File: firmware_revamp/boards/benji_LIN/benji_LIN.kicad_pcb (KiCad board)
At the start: 2 copper layers, 42.9 x 81 mm, 39 parts, among them J1 CONN_02X03, J2 Conn_01x11, J3 Conn_01x11, J4 CONN_01X03, J5 CONN_01x02, J6 CONN_01X03, J7 CONN_01x02, U1 MCP2561-E_SN, U2 ATMEGA16M1, U3 TLIN1021DRQ1, Y1 Crystal_SMD

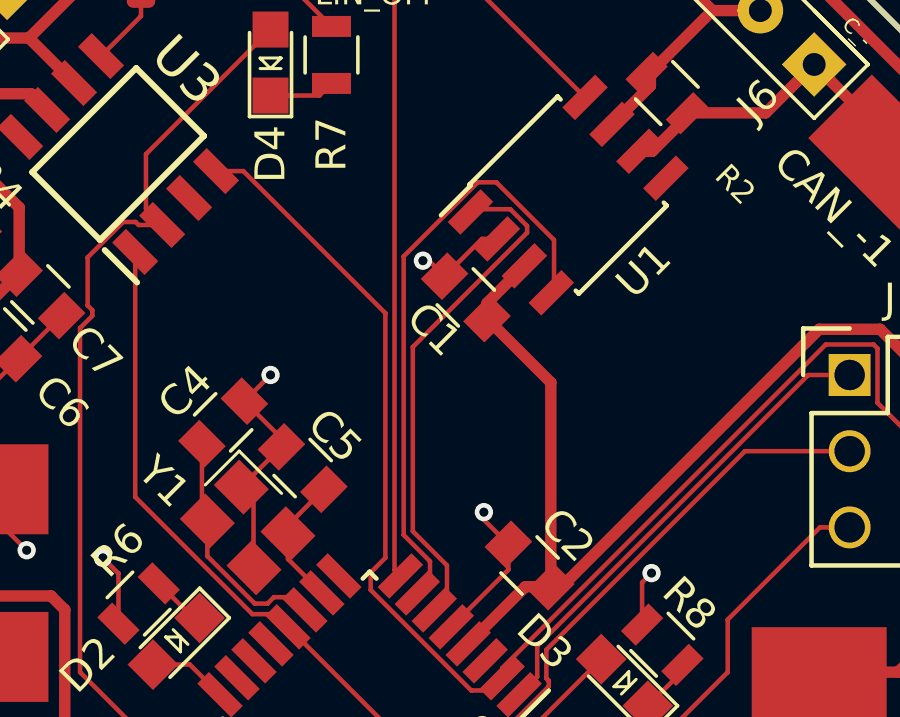
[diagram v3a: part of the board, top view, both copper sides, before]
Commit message: fixed GND via placement
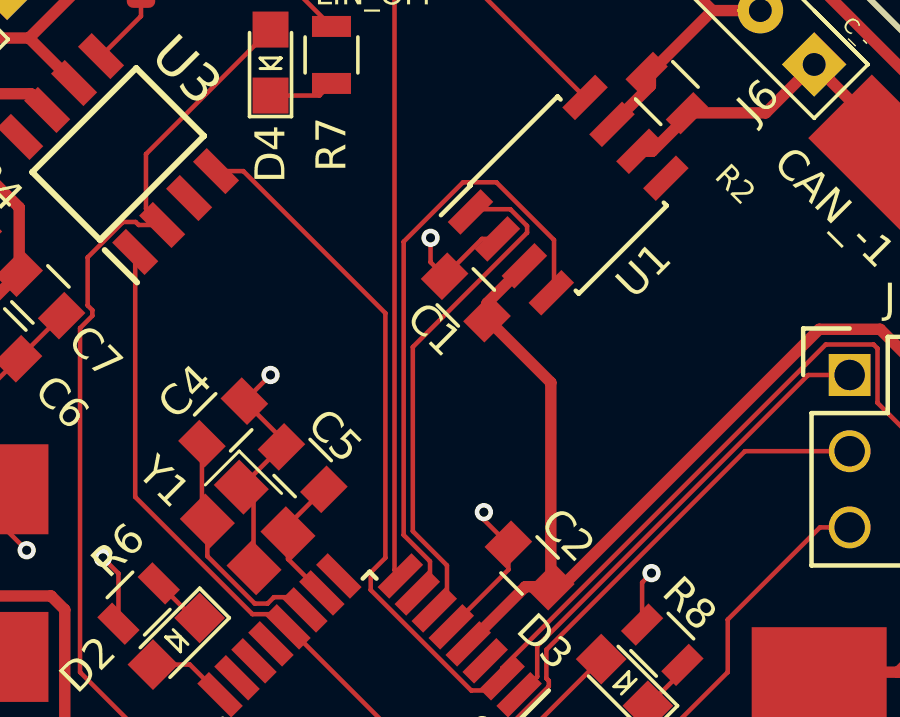
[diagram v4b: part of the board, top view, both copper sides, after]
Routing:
- net GND: track 61.7 -> 62.2 mm
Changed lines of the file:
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@@
   )
   (setup
-    (last_trace_width 0.381)
+    (last_trace_width 0.1524)
     (user_trace_width 0.254)
     (user_trace_width 0.381)
@@
   (via (at 97.028 81.28) (size 0.6096) (drill 0.3048) (layers F.Cu B.Cu) (net 1))
   (via (at 105.156 75.438) (size 0.6096) (drill 0.3048) (layers F.Cu B.Cu) (net 1))
-  (via (at 110.236 71.628) (size 0.6096) (drill 0.3048) (layers F.Cu B.Cu) (net 1))
+  (via (at 110.49 70.866) (size 0.6096) (drill 0.3048) (layers F.Cu B.Cu) (net 1))
   (segment (start 112.203218 70.901485) (end 112.719406 70.901485) (width 0.1524) (layer F.Cu) (net 1))
   (segment (start 110.958003 72.1467) (end 112.203218 70.901485) (width 0.1524) (layer F.Cu) (net 1))
@@
   (segment (start 104.589654 81.845025) (end 104.589654 79.582283) (width 0.1524) (layer F.Cu) (net 1))
   (segment (start 104.606132 81.861503) (end 104.589654 81.845025) (width 0.1524) (layer F.Cu) (net 1))
-  (segment (start 110.439303 71.628) (end 110.958003 72.1467) (width 0.1524) (layer F.Cu) (net 1))
-  (segment (start 110.236 71.628) (end 110.439303 71.628) (width 0.1524) (layer F.Cu) (net 1))
   (segment (start 104.284214 76.309786) (end 105.156 75.438) (width 0.1524) (layer F.Cu) (net 1))
   (segment (start 96.755151 74.896553) (end 98.191992 73.459712) (width 0.1524) (layer F.Cu) (net 1))
@@
   (segment (start 117.541921 82.356079) (end 117.856 82.042) (width 0.1524) (layer F.Cu) (net 1))
   (segment (start 117.541921 83.757746) (end 117.541921 82.356079) (width 0.1524) (layer F.Cu) (net 1))
+  (segment (start 110.49 71.678697) (end 110.958003 72.1467) (width 0.1524) (layer F.Cu) (net 1))
+  (segment (start 110.49 70.866) (end 110.49 71.678697) (width 0.1524) (layer F.Cu) (net 1))
   (segment (start 113.650579 82.495107) (end 111.746047 84.399639) (width 0.381) (layer F.Cu) (net 2))
   (segment (start 114.499107 82.495107) (end 113.650579 82.495107) (width 0.381) (layer F.Cu) (net 2))
@@
   (segment (start 125.73 67.539395) (end 125.73 68.072) (width 0.381) (layer F.Cu) (net 26))
   (segment (start 123.277812 65.087207) (end 125.73 67.539395) (width 0.381) (layer F.Cu) (net 26))
+  (segment (start 109.593661 80.772) (end 110.472055 81.650394) (width 0.1524) (layer F.Cu) (net 28))
+  (segment (start 111.573108 69.01471) (end 109.593661 70.994157) (width 0.1524) (layer F.Cu) (net 28))
+  (segment (start 112.683016 69.01471) (end 111.573108 69.01471) (width 0.1524) (layer F.Cu) (net 28))
   (segment (start 110.472055 81.650394) (end 110.472055 82.279518) (width 0.1524) (layer F.Cu) (net 28))
-  (segment (start 109.593661 80.772) (end 110.472055 81.650394) (width 0.1524) (layer F.Cu) (net 28))
-  (segment (start 112.06256 69.01471) (end 109.593661 71.483609) (width 0.1524) (layer F.Cu) (net 28))
-  (segment (start 112.683016 69.01471) (end 112.06256 69.01471) (width 0.1524) (layer F.Cu) (net 28))
   (segment (start 114.606181 70.937875) (end 112.683016 69.01471) (width 0.1524) (layer F.Cu) (net 28))
   (segment (start 110.472055 82.279518) (end 110.04899 82.702583) (width 0.1524) (layer F.Cu) (net 28))
-  (segment (start 109.593661 71.483609) (end 109.593661 80.772) (width 0.1524) (layer F.Cu) (net 28))
   (segment (start 114.606181 72.606813) (end 114.606181 70.937875) (width 0.1524) (layer F.Cu) (net 28))
+  (segment (start 109.593661 70.994157) (end 109.593661 80.772) (width 0.1524) (layer F.Cu) (net 28))
   (segment (start 114.515457 72.697537) (end 114.606181 72.606813) (width 0.1524) (layer F.Cu) (net 28))
   (segment (start 110.614676 83.187324) (end 110.614676 83.268268) (width 0.1524) (layer F.Cu) (net 29))

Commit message: Finished Ratsnest connections
semifinal version 1.1 commit
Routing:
- net GND: track 62.2 -> 72.8 mm
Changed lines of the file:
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@@
     (thickness 1.6)
     (drawings 22)
-    (tracks 305)
+    (tracks 308)
     (zones 0)
     (modules 39)
@@
   (segment (start 110.49 71.678697) (end 110.958003 72.1467) (width 0.1524) (layer F.Cu) (net 1))
   (segment (start 110.49 70.866) (end 110.49 71.678697) (width 0.1524) (layer F.Cu) (net 1))
+  (segment (start 114.554 102.87) (end 113.284 101.6) (width 0.1524) (layer F.Cu) (net 1))
+  (segment (start 113.284 97.536) (end 116.676249 94.143751) (width 0.1524) (layer F.Cu) (net 1))
+  (segment (start 113.284 101.6) (end 113.284 97.536) (width 0.1524) (layer F.Cu) (net 1))
   (segment (start 113.650579 82.495107) (end 111.746047 84.399639) (width 0.381) (layer F.Cu) (net 2))
   (segment (start 114.499107 82.495107) (end 113.650579 82.495107) (width 0.381) (layer F.Cu) (net 2))

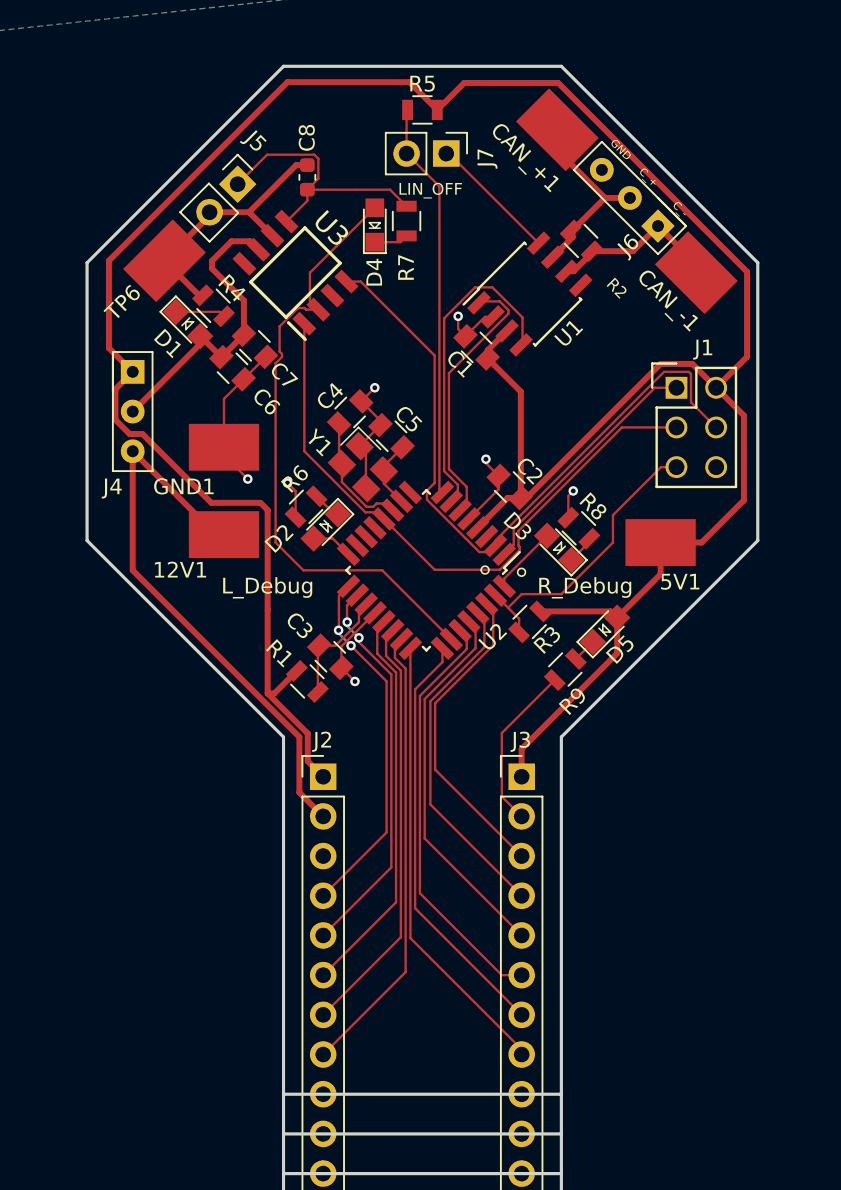
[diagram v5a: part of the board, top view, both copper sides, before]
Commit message: Rearranged mostly visual errors, removed diode
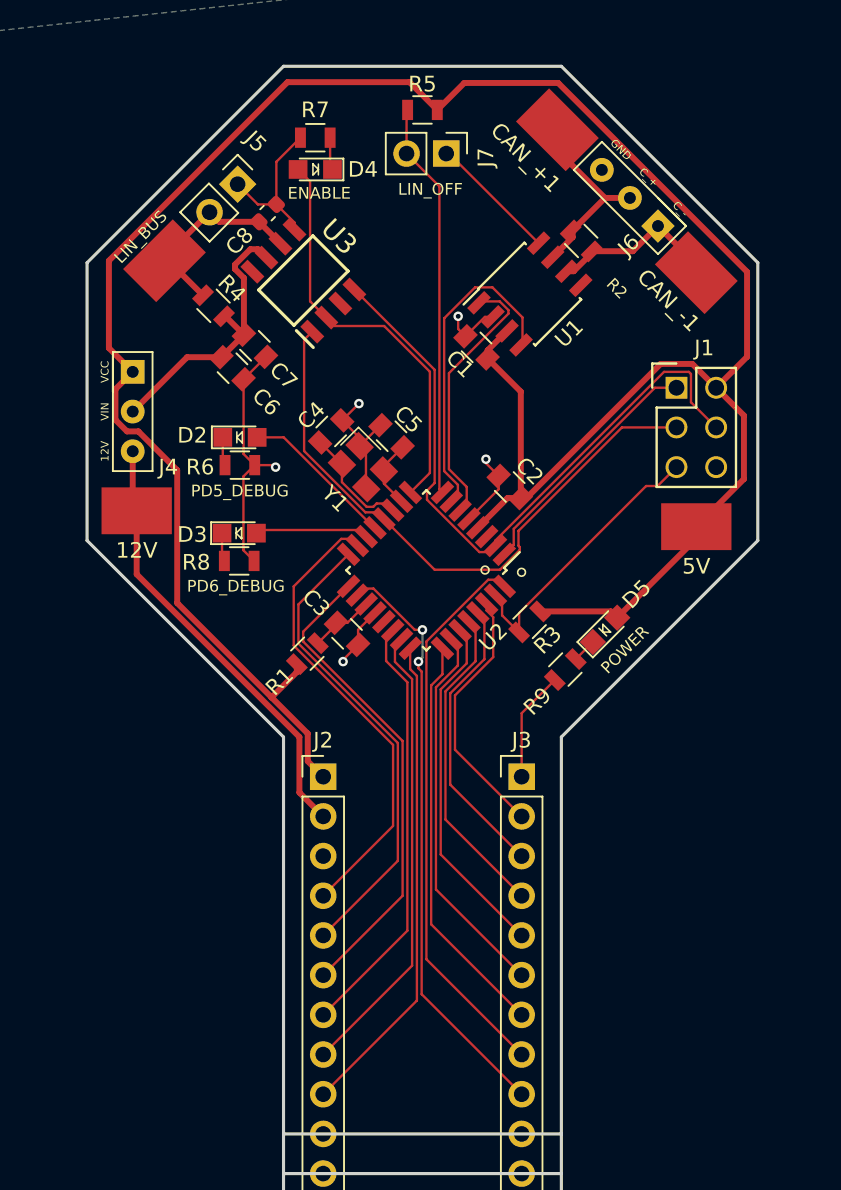
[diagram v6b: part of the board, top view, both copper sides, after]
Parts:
- removed D1: LED_0805, footprints:LED_0805_OEM
- removed GND1: Test_Point_SMD, footprints:Test_Point_SMD
- moved R8 21.8 mm to (96.5, 86.5), turned to 0 degrees
- moved D3 20.5 mm to (96.5, 84.7), turned to 0 degrees
- moved D2 7.91 mm to (96.5, 78.6), turned to 0 degrees
- moved R7 7.91 mm to (101.3, 59.4), turned to 180 degrees
- moved 12V 5.79 mm to (89.9, 83.3)
- moved D4 5.21 mm to (101.3, 61.5), turned to 180 degrees
- moved R6 5.01 mm to (96.5, 80.4), turned to 0 degrees
- moved C8 3.42 mm to (98.3, 64.3), turned to 45 degrees
- moved 5V 2.50 mm to (125.7, 84.3)
- moved C3 1.82 mm to (103.4, 91.2)
- moved R1 1.78 mm to (100.8, 92.5), turned to 45 degrees
- moved C4 1.72 mm to (102.4, 78.2)
- moved U3 0.72 mm to (100.6, 68.6)
- renumbered 12V1 to 12V, 5V1 to 5V, TP6 to LIN_BUS
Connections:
- net /GPIO_10 renamed /PC7
- net /GPIO_4 renamed /PC6
- net /GPIO_5 renamed /PB3
- J2 pad 4: /GPIO_1 -> /PD7
- J2 pad 5: /GPIO_2 -> /PB2
- J2 pad 6: /GPIO_3 -> /PC4
- J2 pad 9: Net-(J2-Pad9) -> /PB4
- J3 pad 1: VCC -> GND
- J3 pad 2: GND -> /PC0
- J3 pad 3: /GPIO_6 -> /PD0
- J3 pad 4: /GPIO_7 -> /PB7
- J3 pad 5: /GPIO_8 -> /PB6
- J3 pad 6: /GPIO_9 -> /PB5
- J3 pad 8: /GPIO_11 -> /PD1
- J3 pad 9: Net-(J3-Pad9) -> /PC5
- R4 pad 1: Net-(D1-Pad1) -> /VIN
- U2 pad 13: Net-(U2-Pad13) -> /LEFT_DEBUG
- U2 pad 14: Net-(U2-Pad14) -> /RIGHT_DEBUG
- U2 pad 15: Net-(U2-Pad15) -> /PD7
- U2 pad 16: /LEFT_DEBUG -> /PB2
- U2 pad 17: /GPIO_1 -> /PC4
- U2 pad 18: /GPIO_2 -> /PC5
- U2 pad 21: /GPIO_3 -> Net-(U2-Pad21)
- U2 pad 24: /GPIO_11 -> /PB4
- U2 pad 26: /ENABLE -> /PB5
- U2 pad 27: /GPIO_9 -> /PB6
- U2 pad 28: /GPIO_8 -> /PB7
- U2 pad 29: /GPIO_7 -> /PD0
- U2 pad 30: /GPIO_6 -> /PC0
- U2 pad 32: /RIGHT_DEBUG -> /PD1
- U2 pad 9: Net-(U2-Pad9) -> /ENABLE
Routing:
- net /PC5: track 0.00 -> 37.9 mm, vias 0 -> 2
- net /PD1: track 0.00 -> 35.8 mm
- net /PB4: track 0.00 -> 31.1 mm
- net /PC4: track 0.00 -> 30.8 mm
- net /PB2: track 0.00 -> 30.3 mm
- net /PD7: track 0.00 -> 29.8 mm
- net /GPIO_11: track 28.6 -> 0.00 mm
- net /GPIO_9: track 26.9 -> 0.00 mm
- net /GPIO_3: track 25.2 -> 0.00 mm
- net /GPIO_2: track 25.0 -> 0.00 mm, vias 2 -> 0
- net /PB5: track 0.00 -> 24.5 mm
- net /GPIO_8: track 24.2 -> 0.00 mm
- net /GPIO_1: track 23.4 -> 0.00 mm, vias 2 -> 0
- net /PB6: track 0.00 -> 22.5 mm
- net /GPIO_7: track 22.1 -> 0.00 mm
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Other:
- outline, holes or cut-outs redrawn
- board text added: "12V"
- board text added: "Benji Pugh"
- board text added: "ENABLE"
- board text added: "PD5_DEBUG"
- board text added: "PD6_DEBUG"
- board text added: "POWER"
- board text added: "V0.2"
- board text added: "VCC"
- board text added: "VIN"
- board text removed: "L_Debug"
- board text removed: "R_Debug"

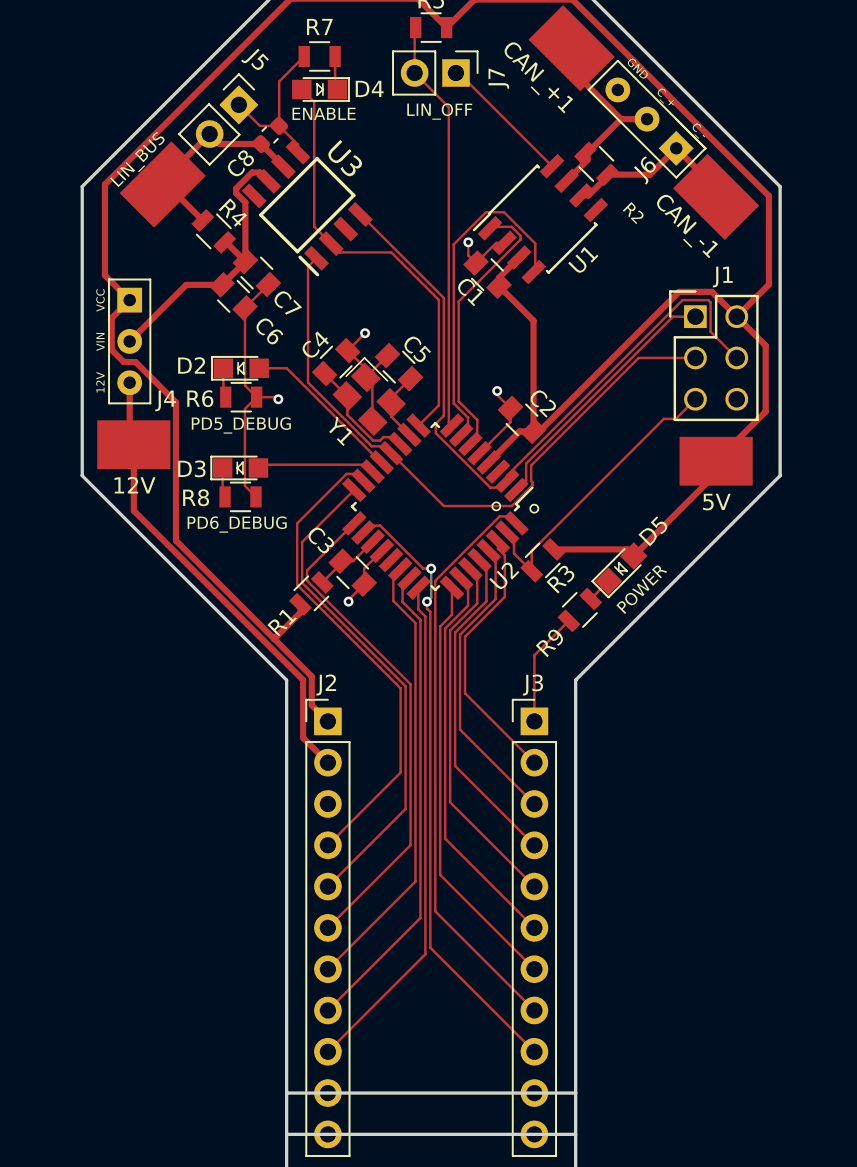
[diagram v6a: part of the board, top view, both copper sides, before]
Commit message: Add labels to headers
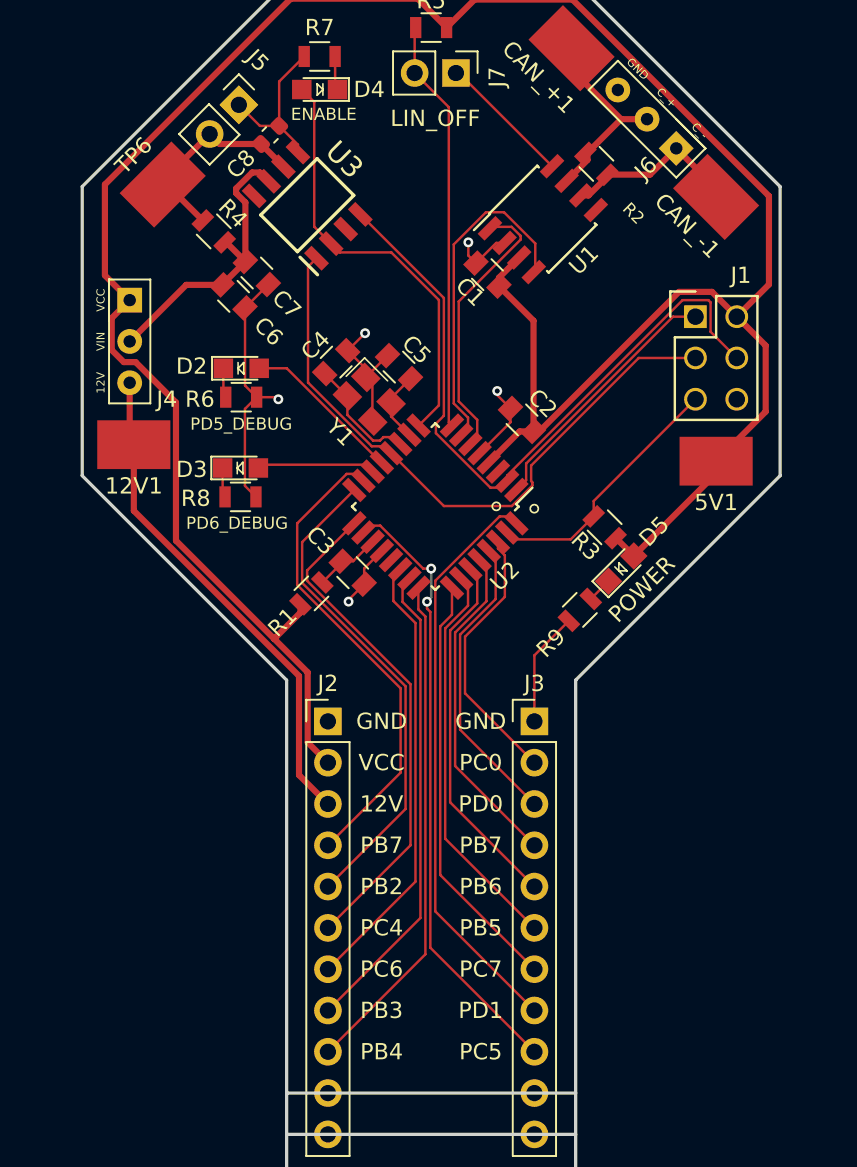
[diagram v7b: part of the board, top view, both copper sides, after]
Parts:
- moved R3 4.32 mm to (118.9, 88.4), turned to 135 degrees
- renumbered 12V to 12V1, 5V to 5V1, LIN_BUS to TP6
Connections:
- J2 pad 1: VCC -> GND
- J2 pad 2: /12V -> VCC
- J2 pad 3: GND -> /12V
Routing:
- net /12V: track 28.4 -> 31.0 mm
- net /RESET: track 18.2 -> 15.9 mm
- net VCC: track 159.3 -> 158.4 mm
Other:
- board text added: "LIN Hackerboard"
- board text added: "Olin Electric Motorsports"
- board text added: "PB2"
- board text added: "PB3"
- board text added: "PB4"
- board text added: "PB5"
- board text added: "PB6"
- board text added: "PB7"
- board text added: "PC0"
- board text added: "PC4"
- board text added: "PC5"
- board text added: "PC6"
- board text added: "PC7"
- board text added: "PD0"
- board text added: "PD1"
- board text added: "V0.3"
- board text removed: "V0.2"
